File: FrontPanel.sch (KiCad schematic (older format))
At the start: 0 parts

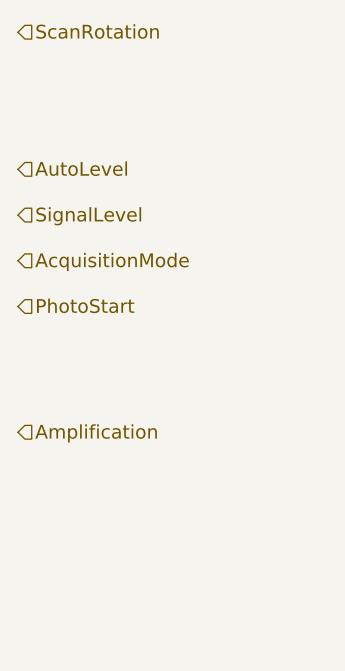
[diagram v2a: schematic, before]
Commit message: Wires up Video Processor Front Panel Control
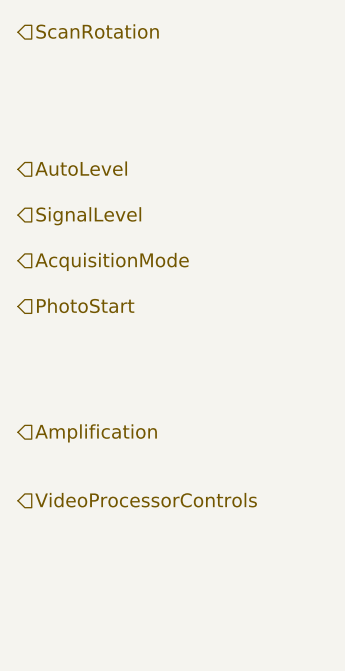
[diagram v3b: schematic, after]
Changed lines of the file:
@@
 Text HLabel 9550 2750 2    60   Input ~ 0
 Amplification
+Text HLabel 9550 3050 2    60   Input ~ 0
+VideoProcessorControls
 $EndSCHEMATC

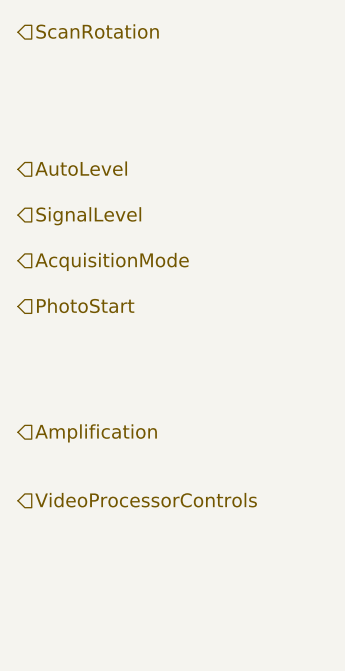
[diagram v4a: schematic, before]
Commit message: Wired up Electron Optics
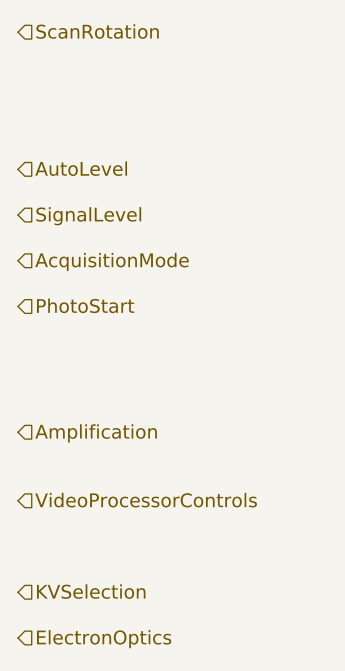
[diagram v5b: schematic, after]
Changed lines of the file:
@@
 Text HLabel 9550 3050 2    60   Input ~ 0
 VideoProcessorControls
+Text HLabel 9550 3450 2    60   Input ~ 0
+KVSelection
+Text HLabel 9550 3650 2    60   Input ~ 0
+ElectronOptics
 $EndSCHEMATC
